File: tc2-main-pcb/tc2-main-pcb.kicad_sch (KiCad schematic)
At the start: 83 parts, among them J101 Conn_02x03_Odd_Even, J102 USB_B_Micro, J103 Conn_01x03, J104 Conn_02x06_Odd_Even, Q101 Q_PMOS_GSD, U101 W25Q128JVS, U102 RP2040, U103 MT29F2G01ABAGDWB-IT, U104 AHT20_C2757850, U105 PCF8563T, U106 M24C02-WMN, Y101 Crystal_GND24, Y102 Crystal

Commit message: Fix library
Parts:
- U101: footprint Package_SO:SOIC-8_5.23x5.23mm_P1.27mm -> Package_SO:SOIC-8_5.3x5.3mm_P1.27mm
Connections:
- net GND: now also J102.SH (Shield); no longer J102.6 (Shield)
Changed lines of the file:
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@@
 	)
 	(junction
+		(at 129.54 124.46)
+		(diameter 0)
+		(color 0 0 0 0)
+	)
+	(junction
 		(at 246.38 49.53)
 		(diameter 0)
@@
 	(wire
 		(pts
-			(xy 139.7 124.46) (xy 140.97 124.46)
-		)
-		(stroke
-			(width 0)
-			(type default)
-		)
-	)
-	(wire
-		(pts
 			(xy 323.85 226.06) (xy 351.79 226.06)
 		)
@@
 	(wire
 		(pts
+			(xy 129.54 124.46) (xy 140.97 124.46)
+		)
+		(stroke
+			(width 0)
+			(type default)
+		)
+	)
+	(wire
+		(pts
 			(xy 40.64 262.89) (xy 41.91 262.89)
 		)
@@
 	)
 	(symbol
-		(lib_name "+3V3_rp2040_3")
 		(lib_id "cacophony-library:+3V3_rp2040")
 		(at 91.44 52.07 0)
@@
 			)
 		)
-		(property "Description" ""
+		(property "Description" "Power symbol creates a global label with name \"+3V3\""
 			(at 91.44 52.07 0)
 			(hide yes)
@@
 			)
 		)
-		(property "Footprint" "Package_SO:SOIC-8_5.23x5.23mm_P1.27mm"
+		(property "Footprint" "Package_SO:SOIC-8_5.3x5.3mm_P1.27mm"
 			(at 78.74 120.65 0)
 			(hide yes)
@@
 			)
 		)
-		(property "Description" ""
+		(property "Description" "Four pin crystal, GND on pins 2 and 4"
 			(at 134.62 124.46 0)
 			(hide yes)
@@
 		(pin "5"
 		)
-		(pin "6"
+		(pin "SH"
 		)
 		(instances
@@
 	)
 	(symbol
-		(lib_name "+3V3_rp2040_2")
 		(lib_id "cacophony-library:+3V3_rp2040")
 		(at 78.74 92.71 0)
@@
 			)
 		)
-		(property "Description" ""
+		(property "Description" "Power symbol creates a global label with name \"+3V3\""
 			(at 78.74 92.71 0)
 			(hide yes)
@@
 			)
 		)
-		(property "Description" ""
+		(property "Description" "Single-cell battery"
 			(at 317.5 232.41 0)
 			(hide yes)
@@
 			)
 		)
+		(property "Sim.Device" "V"
+			(at 317.5 232.41 0)
+			(hide yes)
+			(show_name no)
+			(do_not_autoplace no)
+			(effects
+				(font
+					(size 1.27 1.27)
+				)
+			)
+		)
+		(property "Sim.Type" "DC"
+			(at 317.5 232.41 0)
+			(hide yes)
+			(show_name no)
+			(do_not_autoplace no)
+			(effects
+				(font
+					(size 1.27 1.27)
+				)
+			)
+		)
+		(property "Sim.Pins" "1=+ 2=-"
+			(at 317.5 232.41 0)
+			(hide yes)
+			(show_name no)
+			(do_not_autoplace no)
+			(effects
+				(font
+					(size 1.27 1.27)
+				)
+			)
+		)
 		(pin "1"
 		)
@@
 	)
 	(symbol
-		(lib_name "+3V3_rp2040_1")
 		(lib_id "cacophony-library:+3V3_rp2040")
 		(at 191.77 36.83 0)
@@
 			)
 		)
-		(property "Description" ""
+		(property "Description" "Power symbol creates a global label with name \"+3V3\""
 			(at 191.77 36.83 0)
 			(hide yes)
@@
 	)
 	(symbol
-		(lib_name "+3V3_rp2040_4")
 		(lib_id "cacophony-library:+3V3_rp2040")
 		(at 387.35 127 0)
@@
 			)
 		)
-		(property "Description" ""
+		(property "Description" "Power symbol creates a global label with name \"+3V3\""
 			(at 387.35 127 0)
 			(hide yes)

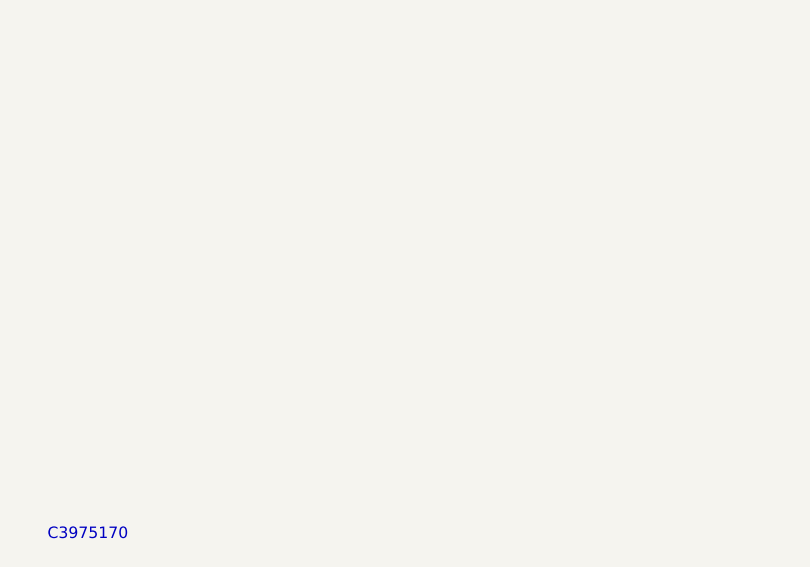
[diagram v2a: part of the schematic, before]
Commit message: Add JLPCPCB 2D barcode to PCBs
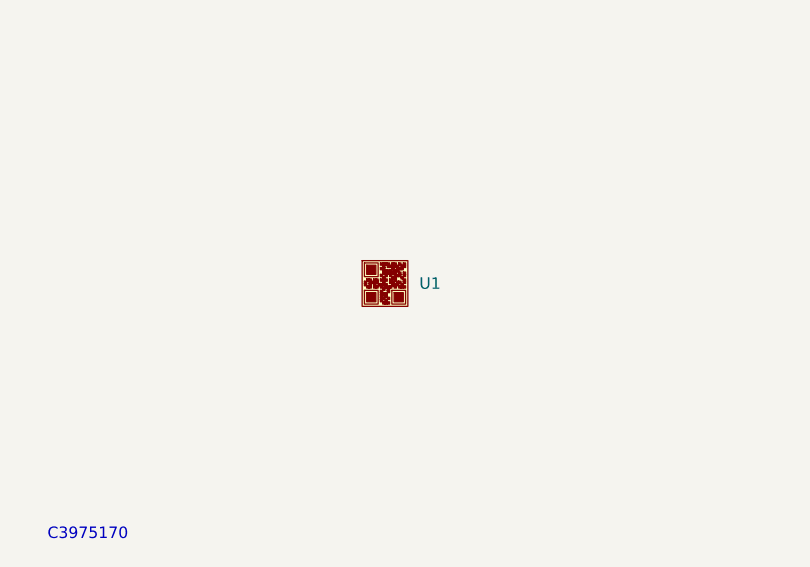
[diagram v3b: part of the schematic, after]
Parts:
- added U1: (no value), cacophony-library:JLCPCB_QR_8mm, symbol cacophony-library:JLCPCB_QR_CODE
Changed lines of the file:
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@@
+	)
+	(symbol
+		(lib_id "cacophony-library:JLCPCB_QR_CODE")
+		(at 81.28 210.82 0)
+		(unit 1)
+		(body_style 1)
+		(exclude_from_sim yes)
+		(in_bom no)
+		(on_board yes)
+		(in_pos_files no)
+		(dnp no)
+		(fields_autoplaced yes)
+		(property "Reference" "U1"
+			(at 85.09 210.8199 0)
+			(show_name no)
+			(do_not_autoplace no)
+			(effects
+				(font
+					(size 1.27 1.27)
+				)
+				(justify left)
+			)
+		)
+		(property "Value" ""
+			(at 81.28 210.82 0)
+			(show_name no)
+			(do_not_autoplace no)
+			(effects
+				(font
+					(size 1.27 1.27)
+				)
+			)
+		)
+		(property "Footprint" "cacophony-library:JLCPCB_QR_8mm"
+			(at 81.28 210.82 0)
+			(hide yes)
+			(show_name no)
+			(do_not_autoplace no)
+			(effects
+				(font
+					(size 1.27 1.27)
+				)
+			)
+		)
+		(property "Datasheet" ""
+			(at 81.28 210.82 0)
+			(hide yes)
+			(show_name no)
+			(do_not_autoplace no)
+			(effects
+				(font
+					(size 1.27 1.27)
+				)
+			)
+		)
+		(property "Description" ""
+			(at 81.28 210.82 0)
+			(hide yes)
+			(show_name no)
+			(do_not_autoplace no)
+			(effects
+				(font
+					(size 1.27 1.27)
+				)
+			)
+		)
+		(instances
+			(project "tc2-main-pcb"
+				(path "/0662f88c-5300-4b75-bef3-048a3227af84"
+					(reference "U1")
+					(unit 1)
+				)
+			)
+		)
 	)
 	(symbol

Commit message: Update schematic
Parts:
- removed D102: D, Diode_SMD:D_SOD-523, symbol Device:D
- removed R113: 1k, Resistor_SMD:R_0402_1005Metric, symbol Device:R
- added J1901: TC2030, cacophony-library:Tag-Connect_TC2030-IDC-NL_2x03_P1.27mm_Vertical, symbol Connector:TC2030
- added R1: 10M, Resistor_SMD:R_0402_1005Metric, symbol Device:R
- added R117, R129, R131, R136: 10k, Resistor_SMD:R_0402_1005Metric, symbol Device:R
- added TP120, TP121: TestPoint, TestPoint:TestPoint_Pad_D1.0mm, symbol Connector:TestPoint
- BT101: value Battery_Cell -> MS621FE-FL11E
- C101, C102, C103, C104, C105, C106, C107, C108, C109, C112, C113, C114, C117, C118: symbol Device:C -> Device:C_Small
- C123: value 22pF -> 220nF; LCSC Part C1555 -> C16772
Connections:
- net +3V3: now also R131.1, R136.1; no longer R105.1, R107.1
- net +3V3_rp2040: now also R105.1, R107.1, R117.1, R129.1
- net EEPROM_~{WC}: now also J1901.1
- net GND: now also J1901.5
- net RTC_BATTERY: now also R1.2
- net RTC_BT_SENSE_PHY: now also C123.1, R1.1
- net RTC_OSCO: no longer C123.1
- net SCL: now also J1901.4, R129.2, R136.2
- net SDA: now also J1901.2, R117.2, R131.2
- new net: J1901.3, TP121.1
- new net: J1901.6, TP120.1
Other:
- note added: "This capacitor should be close to pin 44 of RP2040"
- note removed: "EEPROM 2K"
- note removed: "I2C Address 0x38"
- note removed: "I2C Address 0x50"
- note removed: "I2C Address 0x51"
- note removed: "Make sure C10 is close to pin 44 of RP2040"
- note removed: "Microphone Connector"
- note removed: "RTC"
- note removed: "Temp and Humidity Sensor"
- moved on the sheet: BT101, C101, C102, C103, C104, C105, C106, C107, C108, C109, C110, C111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

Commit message: Update layout
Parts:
- removed TP105: TestPoint, cacophony-library:TP, symbol Connector:TestPoint
- removed TP117: TestPoint, TestPoint:TestPoint_Pad_D1.0mm, symbol Connector:TestPoint
- TP104, TP106, TP107: footprint cacophony-library:TP -> TestPoint:TestPoint_Loop_D2.54mm_Drill1.5mm_Beaded
